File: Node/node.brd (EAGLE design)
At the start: 160 x 100 mm, 33 parts, among them SW1 SWITCH-MOMENTARY-2PTH, SW2 SWITCH-MOMENTARY-2PTH, SW3 SWITCH-MOMENTARY-2PTH, U1 FT232RLSSOP, U2 DW1000-I, U4 ATMEGA328, X2 332-02, Y1 8MHz

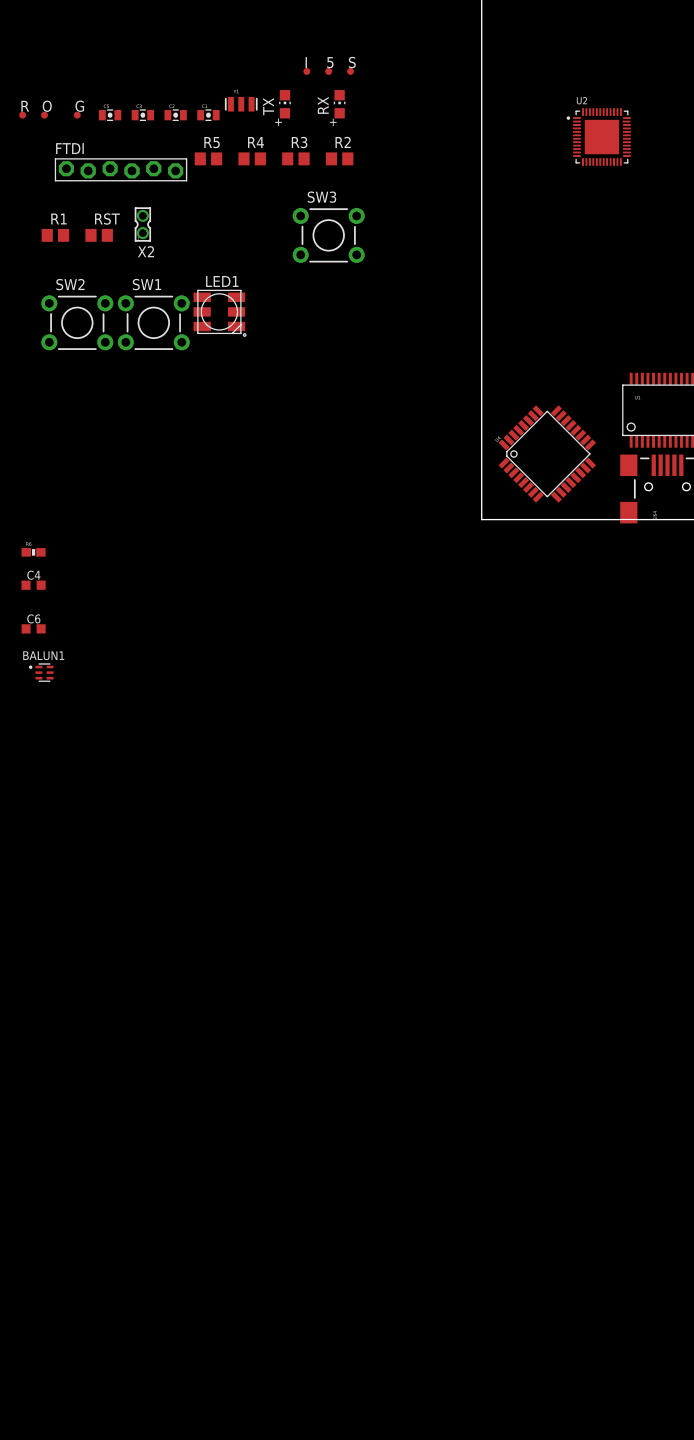
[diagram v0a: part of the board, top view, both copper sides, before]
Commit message: Work on the DW1000 SCH
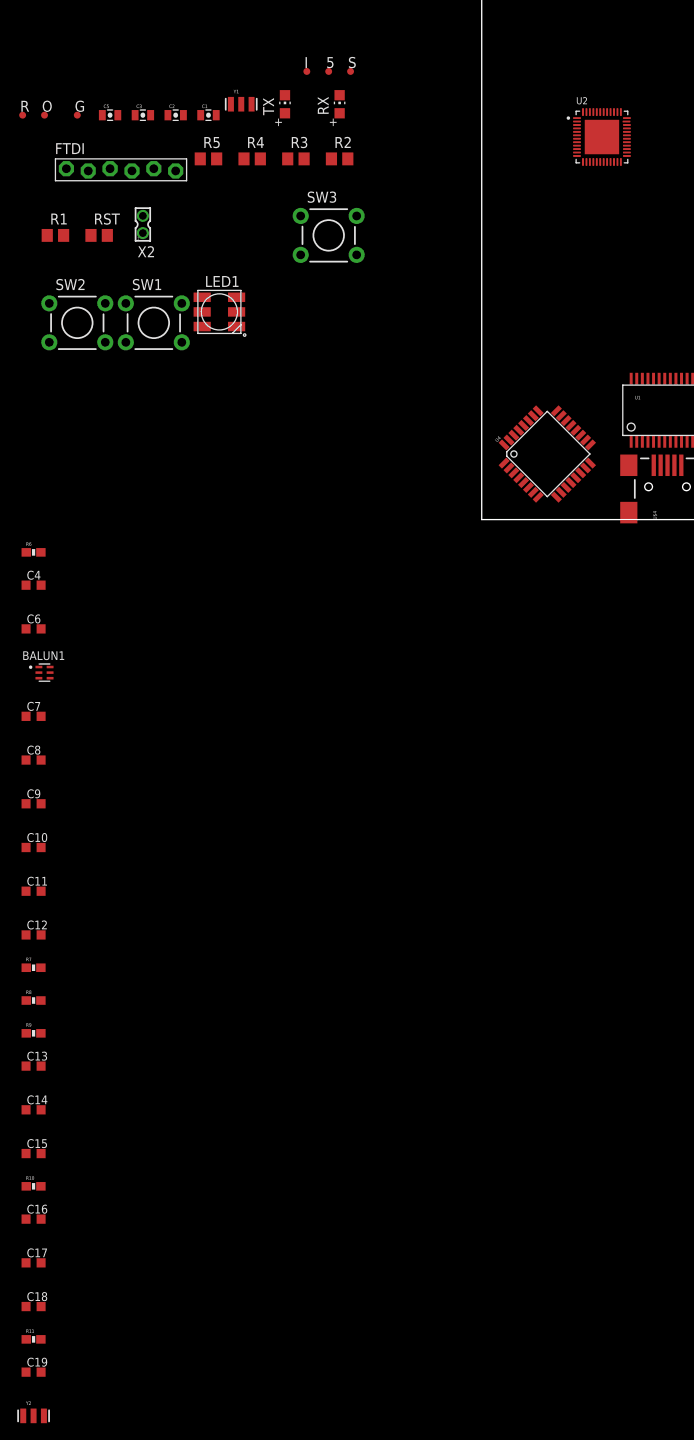
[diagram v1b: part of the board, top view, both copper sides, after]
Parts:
- added C10, C11, C12, C17, C7, C8, C9: 0.1uF, adafruit:C0603K
- added C13, C14: 12pf, adafruit:C0603K
- added C15: 18pF, adafruit:C0603K
- added C16: 820pF, adafruit:C0603K
- added C18: 1p2, adafruit:C0603K
- added C19: 27pF, adafruit:C0603K
- added R10: 270, SparkFun-Resistors:0603-RES
- added R11: 16k, SparkFun-Resistors:0603-RES
- added R7: 100K, SparkFun-Resistors:0603-RES
- added R8, R9: 10k, SparkFun-Resistors:0603-RES
- added Y2: 38.4MHz, 10pF, SparkFun-FreqCtrl:RESONATOR-SMD
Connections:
- removed net VDDAON: U2.25
- removed net VDDBATT: U2.47
- removed net VDDIOA: U2.28
- removed net VDDLDOA: U2.48
- removed net VDDLDOD: U2.26
- removed net VDDLNA: U2.15
- removed net VDDPA1: U2.18
- removed net VDDPA2: U2.19
- removed net VDDREG: U2.20
- new net !RST: U2.27
- new net !SPICS: U2.24
- new net EXTON: U2.21
- new net GPIO0: U2.38
- new net GPIO1: U2.37
- new net GPIO2: U2.36
- new net GPIO3: U2.35
- new net GPIO4: U2.34
- new net GPIO5: R8.2, U2.33
- new net GPIO6: R9.2, U2.30
- new net N$10: C10.1, U2.20, U2.44
- new net N$11: C18.2, R11.2, U2.8
- new net N$12: U2.4, Y2.3
- new net N$13: U2.3, Y2.1
- new net N$14: C19.2, R11.1
- new net N$16: R7.2, U2.45
- new net RF_N: C14.2, U2.17
- new net RF_P: C13.2, U2.16
- new net SPICLK: U2.41
- new net SPIMISO: U2.40
- new net SPIMOSI: U2.39
- new net SYNC: U2.29
- new net VCOTUNE: C15.2, R10.2, U2.12
- new net VDDIO: C17.1, C4.1, R8.1, R9.1, U2.31, U2.42
- new net WAKEUP: U2.23
- net 3.3V: now also U2.15, U2.18, U2.19, U2.25, U2.26, U2.28, U2.47, U2.48; no longer U2.44
- net GND: now also C10.2, C11.2, C12.2, C17.2, C7.2, C8.2, C9.2, R7.1, Y2.2
- net N$7: now also C16.2, R10.1; no longer C4.1, U2.31, U2.42
- net VDDCLK: now also C18.1, C19.1, C7.1
- net VDDIF: now also C9.1
- net VDDMS: now also C8.1
- net VDDSYN: now also C12.1
- net VDDVCO: now also C11.1, C15.1, C16.1

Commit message: Added some required ground connections
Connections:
- net GND: now also U2.22, U2.46
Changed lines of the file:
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@@
 <contactref element="C17" pad="2"/>
 <contactref element="Y2" pad="2"/>
+<contactref element="U2" pad="46"/>
+<contactref element="U2" pad="22"/>
 <wire x1="-51.195" y1="-86.36" x2="-52.07" y2="-104.14" width="0" layer="19" extent="1-1"/>
 <wire x1="-52.92" y1="-52.07" x2="-51.195" y2="-86.36" width="0" layer="19" extent="1-1"/>
@@
 <wire x1="-41.3512" y1="25.1206" x2="-50.2412" y2="25.1206" width="0" layer="19" extent="1-1"/>
 <wire x1="-39.37" y1="33.29" x2="-41.3512" y2="25.1206" width="0" layer="19" extent="1-1"/>
-<wire x1="13.97" y1="44.45" x2="-17.46" y2="41.91" width="0" layer="19" extent="1-1"/>
-<wire x1="13.77" y1="47.35" x2="13.97" y2="44.45" width="0" layer="19" extent="1-1"/>
+<wire x1="12.57" y1="47.35" x2="-17.46" y2="41.91" width="0" layer="19" extent="1-1"/>
+<wire x1="13.77" y1="47.35" x2="12.57" y2="47.35" width="0" layer="19" extent="1-1"/>
+<wire x1="13.97" y1="44.45" x2="13.77" y2="47.35" width="0" layer="19" extent="1-1"/>
 <wire x1="16.87" y1="45.05" x2="13.97" y2="44.45" width="0" layer="19" extent="1-1"/>
-<wire x1="18.665" y1="16.356" x2="13.97" y2="44.45" width="0" layer="19" extent="1-1"/>
+<wire x1="15.37" y1="41.55" x2="13.97" y2="44.45" width="0" layer="19" extent="1-1"/>
+<wire x1="18.665" y1="16.356" x2="15.37" y2="41.55" width="0" layer="19" extent="1-1"/>
 <wire x1="19.315" y1="16.356" x2="18.665" y2="16.356" width="0" layer="19" extent="1-1"/>
 <wire x1="21.915" y1="16.356" x2="19.315" y2="16.356" width="0" layer="19" extent="1-1"/>

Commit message: More work on schematic, documentation, frame, shielding, etc.
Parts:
- added C20: 0.1uF, SparkFun-Passives:0603-CAP
- added C20-VDDLNA: 10nF, SparkFun-Passives:0603-CAP
- added J1: U.FL, SparkFun-Connectors:U.FL
- added S1: WE-SHC_36103305, Wurth_Elektronik_Passive_rev15e:WE-SHC_36103305
- added TP1, TP2, TP3-OTP: TEST-POINT3X4, SparkFun-Passives:PAD.03X.04
- C10, C11, C12, C13, C14, C15, C16, C17, C18, C19, C4, C6, C7, C8, C9: device adafruit:C0603K -> SparkFun-Passives:0603-CAP
- Y1: value 8MHz -> 4MHz; device SparkFun-FreqCtrl:RESONATOR-SMD -> SparkFun-FreqCtrl:RESONATOR-SMD_MED
- Y2: value 38.4MHz, 10pF -> 4MHz; device SparkFun-FreqCtrl:RESONATOR-SMD -> SparkFun-FreqCtrl:RESONATOR-SMD_MED
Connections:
- new net ANT: BALUN1.1, J1.P$3
- new net BAL_3: BALUN1.3, C14.1
- new net BAL_4: BALUN1.4, C13.1
- net 3.3V: now also C20-VDDLNA.1
- net GND: now also C20-VDDLNA.2, C20.1, S1.1
- net GPIO5: now also TP1.P$1
- net GPIO6: now also TP2.P$1
- net VDDIO: now also C20.2, TP3-OTP.P$1

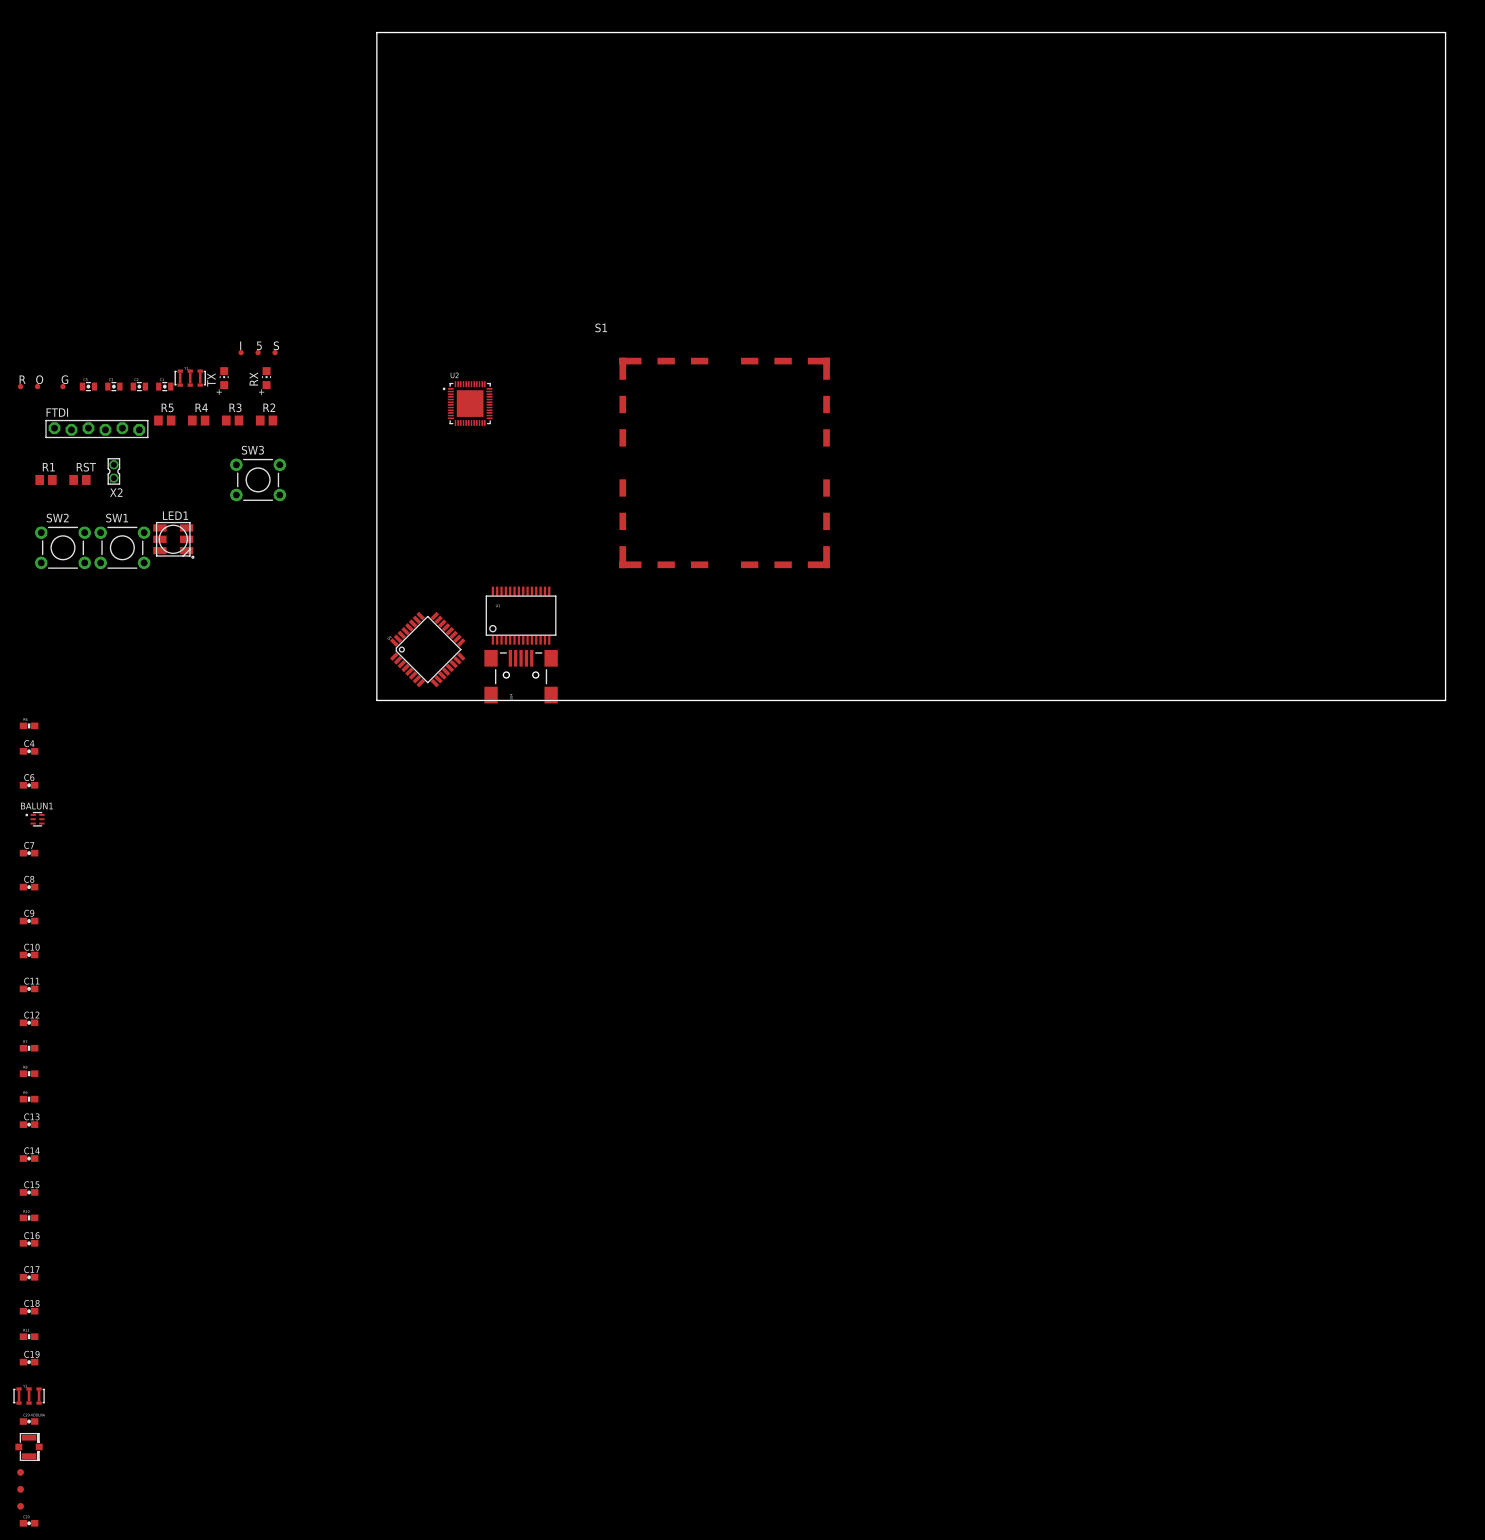
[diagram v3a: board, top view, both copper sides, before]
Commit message: Moved the RF components to an area that will be covered by the RF shield. Also went through two sources and confirmed SCH and BRD layout for the DW1000 (specifically with respect to caps and resistors). Also Added the correct IO to and from the ATMEGA
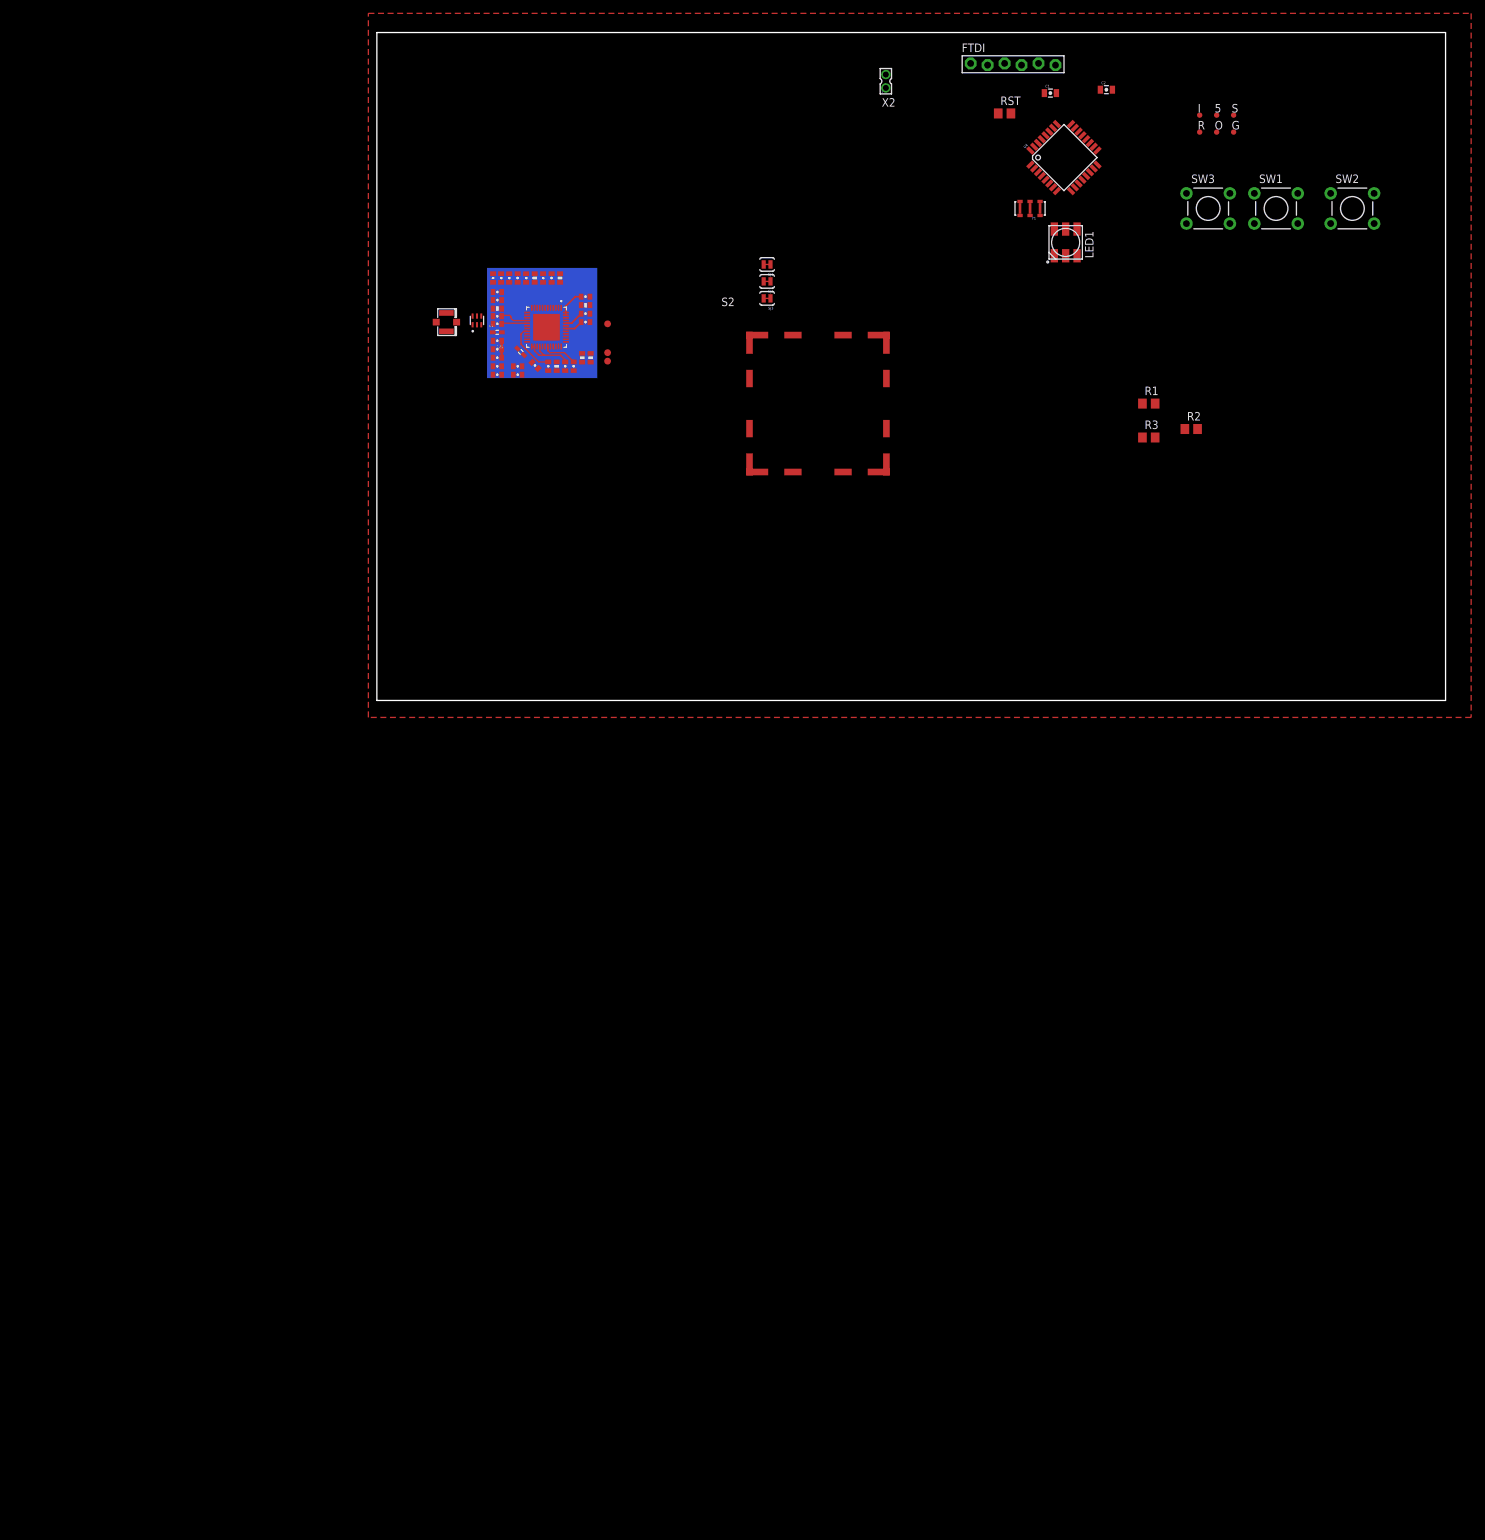
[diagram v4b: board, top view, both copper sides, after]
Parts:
- removed C17, C6: 0.1uF, SparkFun-Passives:0603-CAP
- removed C20-VDDLNA: 10nF, SparkFun-Passives:0603-CAP
- removed R5: 150, resistor:R0805
- removed RX: R, adafruit:CHIP-LED0805
- removed S1: WE-SHC_36103305, Wurth_Elektronik_Passive_rev15e:WE-SHC_36103305
- removed TX: G, adafruit:CHIP-LED0805
- removed U$4: USB-MINIB-5PIN, SparkFun-Connectors:USB-MINIB
- removed U1: FT232RLSSOP, SparkFun:SSOP28DB
- removed Y2: 4MHz, SparkFun-FreqCtrl:RESONATOR-SMD_MED
- added C21: 0.1uF, SparkFun-Passives:0402-CAP
- added C23, C27: 12nF, SparkFun-Passives:0402-CAP
- added C24, C28: 330nF, SparkFun-Passives:0402-CAP
- added C25, C29: 100nF, SparkFun-Passives:0402-CAP
- added C26: 47uF, SparkFun-Passives:0402-CAP
- added C31: 22uF, SparkFun-Passives:0402-CAP
- added L1, L2: BLM15AG601SN1D, Wurth_Elektronik_Passive_rev15e:WE-CBA_0402(W=2.2)
- added S2: WE-SHC_36103205, Wurth_Elektronik_Passive_rev15e:WE-SHC_36103205
- added SJ1, SJ2, SJ3: SOLDERJUMPERTRACE, SparkFun-Retired:SJ_2S-TRACE
- C10, C11, C12, C13, C14, C15, C16, C18, C19, C20, C4, C7, C8, C9: device SparkFun-Passives:0603-CAP -> SparkFun-Passives:0402-CAP
- C3, C5: value 1.0uF -> 0.1uF; device SparkFun-Capacitors:0805-CAP -> SparkFun-Passives:0402-CAP
- R1, R2, R3: value 150 -> 100
- R10, R11, R6, R7, R8, R9: device SparkFun-Resistors:0603-RES -> SparkFun-Passives:0402-RES
- R4: value 150 -> 10K; device resistor:R0805 -> SparkFun-Passives:0402-RES
- Y1: value 4MHz -> 8MHz
- moved SW2 199.6 mm to (146.1, 73.7)
- moved C20 198.2 mm to (31.2, 56.6), turned to 180 degrees
- moved TP3-OTP 197.7 mm to (34.5, 56.4), turned to 90 degrees
- moved TP2 190.4 mm to (34.5, 50.8), turned to 90 degrees
- moved TP1 189.3 mm to (34.5, 52.1), turned to 90 degrees
- moved O 180.6 mm to (125.7, 85.1)
- moved R 180.6 mm to (123.2, 85.1)
- moved SW1 180.0 mm to (134.6, 73.7)
- moved J1 179.6 mm to (10.4, 56.6)
- moved G 179.4 mm to (128.3, 85.1)
- moved C19 178.6 mm to (22.4, 63.2), turned to 270 degrees
- moved R11 175.6 mm to (23.6, 63.2), turned to 270 degrees
- moved C18 171.1 mm to (21.1, 63.2), turned to 270 degrees
- moved R1 165.5 mm to (115.6, 44.5)
- moved C16 157.7 mm to (18.0, 59.9), turned to 180 degrees
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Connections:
- net A_ALT renamed D7
- net A_SPD renamed A6
- net B_ALT renamed D8
- net B_SPD renamed A7
- net N$11 renamed CLKTUNE
- net N$8 renamed VREF
- net SCL renamed A5
- net SDA renamed A4
- net SW1 renamed A3
- net SW3 renamed D10
- net S_ALT renamed A2
- net S_HDG renamed A1
- removed net 5V: 5.TP, C3.1, FTDI.3, RST.2, RX.A, TX.A, U$4.VBUS, U1.20, U1.4, U4.18, U4.4, U4.6
- removed net A_HDG: U4.2
- removed net B_HDG: U4.9
- removed net IO13: S.TP, U4.17
- removed net N$12: U2.4, Y2.3
- removed net N$13: U2.3, Y2.1
- removed net N$5: R5.2, RX.C
- removed net N$6: R4.2, TX.C
- removed net RXI: FTDI.5, U1.5, U4.31
- removed net RXLED: R5.1, U1.22
- removed net S-RX: I.TP, U4.16
- removed net S-TX: O.TP, U4.15
- removed net SW2: SW2.3, U4.32
- removed net S_SPD: U4.23
- removed net TXLED: R4.1, U1.23
- removed net TXO: FTDI.4, U1.1, U4.30
- removed net USB_D+: U$4.D+, U1.15
- removed net USB_D-: U$4.D-, U1.16
- new net D2: SW2.3
- new net MISO: I.TP, SJ2.1, U4.16
- new net MOSI: O.TP, SJ3.1, U4.15
- new net RXD: FTDI.4, U4.30
- new net SCK: S.TP, SJ1.1, U4.17
- new net TXD: FTDI.5, U4.31
- new net VDDPA1: C23.1, C24.1, C25.1, L1.1, U2.18
- new net VDDPA2: C27.1, C28.1, C29.1, C31.1, L2.1, U2.19
- net !RST: now also U4.2
- net !SPICS: now also U4.32
- net 3.3V: now also 5.TP, C21.1, C26.2, C3.1, FTDI.3, L1.2, L2.2, RST.2, U4.18, U4.4, U4.6; no longer C20-VDDLNA.1, C5.1, C6.1, U1.17, U2.18, U2.19
- net DTR: no longer U1.2
- net EXTON: now also U4.23
- net GND: now also C21.2, C23.2, C24.2, C25.2, C26.1, C27.2, C28.2, C29.2, C31.2, J1.P$1, J1.P$2, R4.2, S2.1; no longer C17.2, C20-VDDLNA.2, C6.2, S1.1, U$4.GND, U$4.MTN1, U$4.MTN2, U$4.MTN3, U$4.MTN4, U1.18, U1.21, U1.25, U1.26, U1.7, Y2.2
- net N$10: now also C5.1
- net SPICLK: now also SJ1.2
- net SPIMISO: now also SJ2.2
- net SPIMOSI: now also SJ3.2
- net VDDIO: no longer C17.1
- net WAKEUP: now also R4.1, U4.9
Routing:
- net 3.3V: track 0.00 -> 12.3 mm
- net N$10: track 0.00 -> 10.7 mm
- net VDDIO: track 0.00 -> 8.11 mm
- net RF_P: track 0.00 -> 4.39 mm
- net RF_N: track 0.00 -> 3.85 mm
- net VDDPA1: track 0.00 -> 2.54 mm
- added copper zone on layer 1, net GND
